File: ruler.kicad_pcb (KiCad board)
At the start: 2 copper layers, 170.8 x 38.1 mm, 25 parts, among them J1 USB_OTG, J2 Conn_01x01, SW1 KMR2, SW2 EVQPE1, SW3 B3U1000P, SW4 FSMCT, SW5 TL3315, SW6 FSM2JSM, SW7 JS202011SCQN

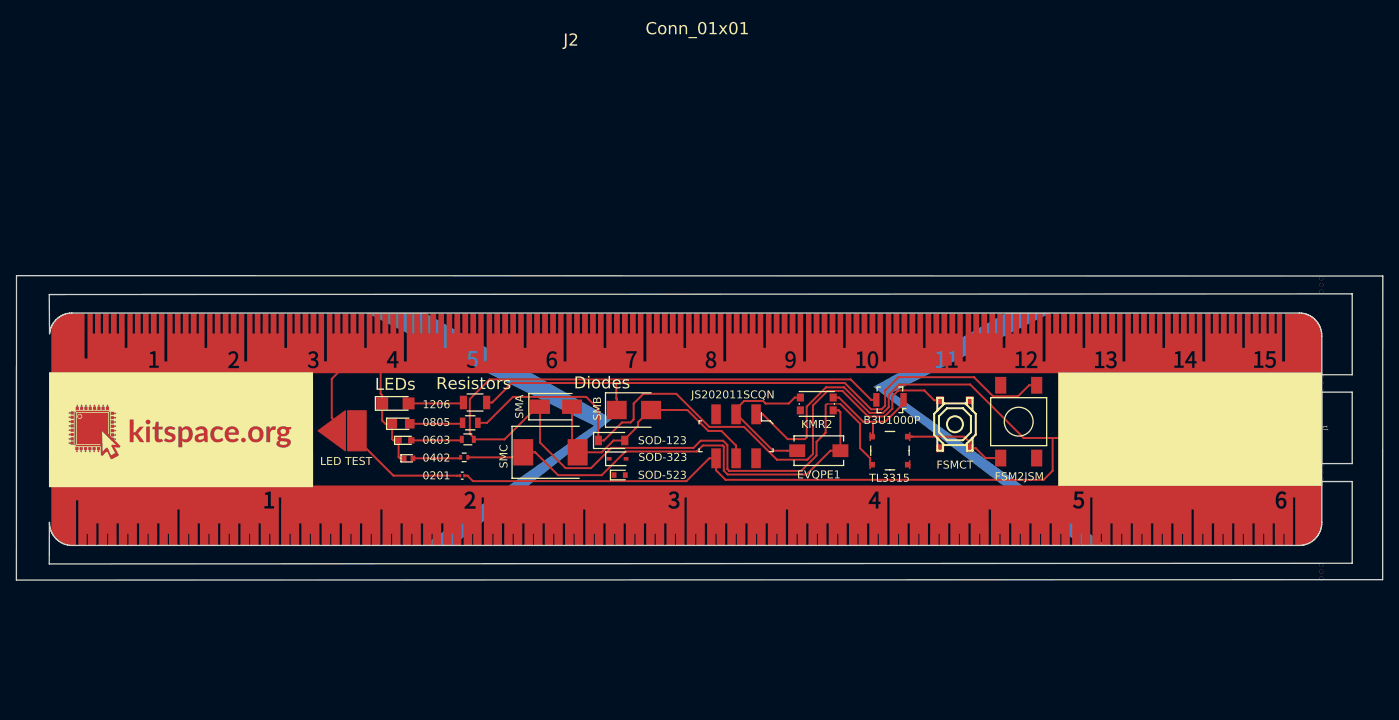
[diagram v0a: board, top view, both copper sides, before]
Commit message: Add inductors, caps, transitors and ICs
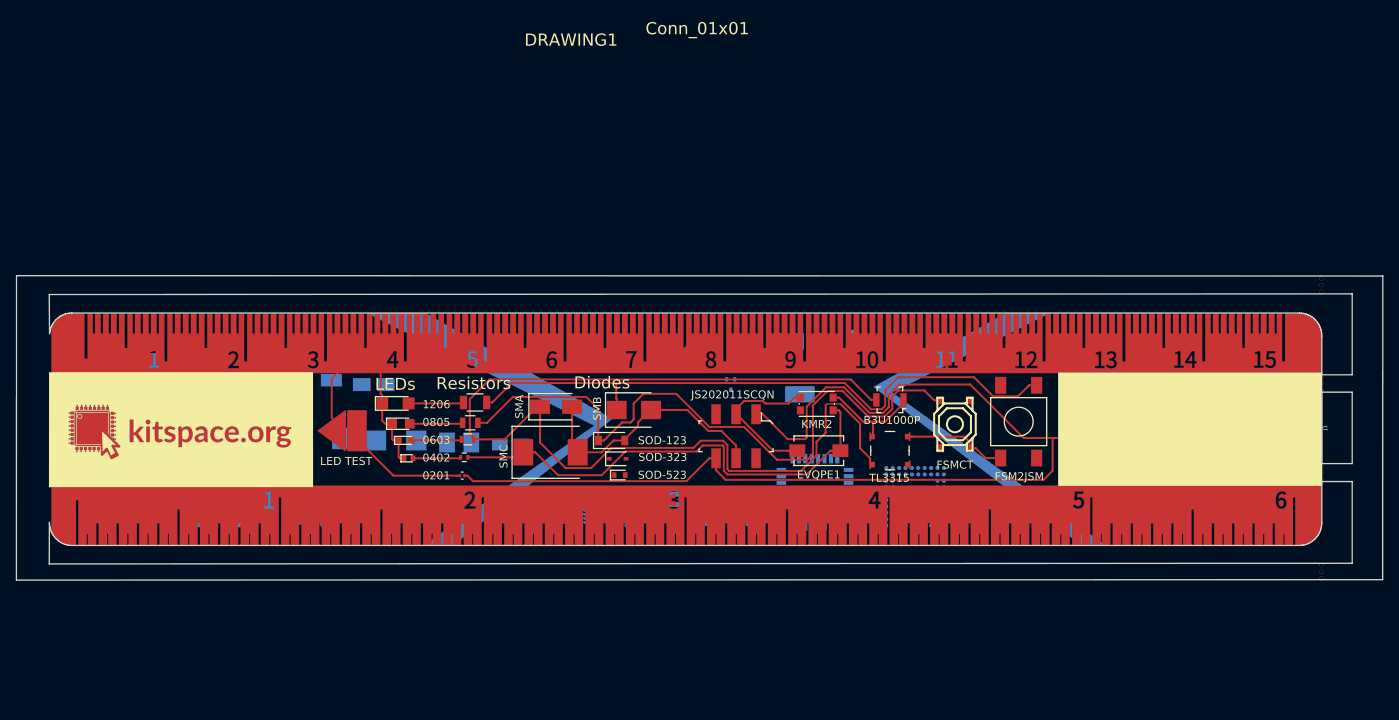
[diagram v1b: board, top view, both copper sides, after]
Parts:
- removed J2: Conn_01x01, drawing:drawing
- added C1: 3x5.3mm, KiCad/Capacitors_SMD.pretty:CP_Elec_3x5.3, B.Cu at (105.9, 99.5)
- added C2: 4x5.8mm, KiCad/Capacitors_SMD.pretty:CP_Elec_4x5.8, B.Cu at (98.8, 98.9)
- added C3: 5x5.8mm, KiCad/Capacitors_SMD.pretty:CP_Elec_5x5.8, B.Cu at (90.7, 98.5)
- added C4: 8x5.4mm, KiCad/Capacitors_SMD.pretty:CP_Elec_8x5.4, B.Cu at (80.8, 96.8)
- added C5: A/3216, KiCad/Capacitors_Tantalum_SMD.pretty:CP_Tantalum_Case-A_EIA-3216-18_Reflow, B.Cu at (123.0, 106.9)
- added C6: B/3528, KiCad/Capacitors_Tantalum_SMD.pretty:CP_Tantalum_Case-B_EIA-3528-21_Reflow, B.Cu at (116.6, 106.7)
- added C7: C/6032, KiCad/Capacitors_Tantalum_SMD.pretty:CP_Tantalum_Case-C_EIA-6032-28_Reflow, B.Cu at (108.7, 106.4)
- added C8: D/7343, KiCad/Capacitors_Tantalum_SMD.pretty:CP_Tantalum_Case-D_EIA-7343-31_Reflow, B.Cu at (98.8, 106.2)
- added DRAWING1: Conn_01x01, drawing:drawing, F.Cu at (148.5, 105.0)
- added L1: 1008, jnedbal/jakub.pretty:Inductor_1008, B.Cu at (106.7, 116.5)
- added L2: SRU8043, custom:Inductor_Bourns-SRU8043, B.Cu at (77.0, 113.2)
- added L3: 4040, KiCad/Inductors.pretty:Inductor_Taiyo-Yuden_MD-4040, B.Cu at (101.2, 115.3)
- added L4: 5050, KiCad/Inductors.pretty:Inductor_Taiyo-Yuden_MD-5050, B.Cu at (94.7, 114.8)
- added L5: 60xx, KiCad/Inductors.pretty:Inductor_Taiyo-Yuden_NR-60xx, B.Cu at (87.0, 114.3)
- added Q1: Q_NMOS_DGS, adamgreig/agg-kicad/agg.pretty:SOT-23, B.Cu at (166.8, 93.8)
- added Q2: Q_NMOS_DGS, adamgreig/agg-kicad/agg.pretty:SOT-323, B.Cu at (144.2, 95.0)
- added Q3: Q_NMOS_DGS, adamgreig/agg-kicad/agg.pretty:SOT-883-B, B.Cu at (151.4, 93.8)
- added Q4: Q_NMOS_DGS, digikey/digikey-kicad-library/digikey-footprints.pretty:SOT-523, B.Cu at (150.5, 98.8)
- added Q5: Q_NMOS_DGS, ep092/library_toni.pretty:SOT223_GND_VO_VI, B.Cu at (159.2, 97.3)
- added U1: Conn_01x01, KiCad/Housings_DFN_QFN.pretty:QFN-16-1EP_3x3mm_Pitch0.5mm, B.Cu at (131.0, 115.9)
- added U2: Conn_01x01, adamgreig/agg-kicad/agg.pretty:LQFP-32, B.Cu at (161.1, 112.9)
- added U3: Conn_01x01, adamgreig/agg-kicad/agg.pretty:SOIC-8, B.Cu at (140.8, 115.0)
- added U4: Conn_01x01, KiCad/SMD_Packages.pretty:BGA-64-0.8mm, B.Cu at (173.6, 113.5)
- added U5: Conn_01x01, KiCad/Housings_SSOP.pretty:TSSOP-16_4.4x5mm_Pitch0.65mm, B.Cu at (150.2, 114.6)

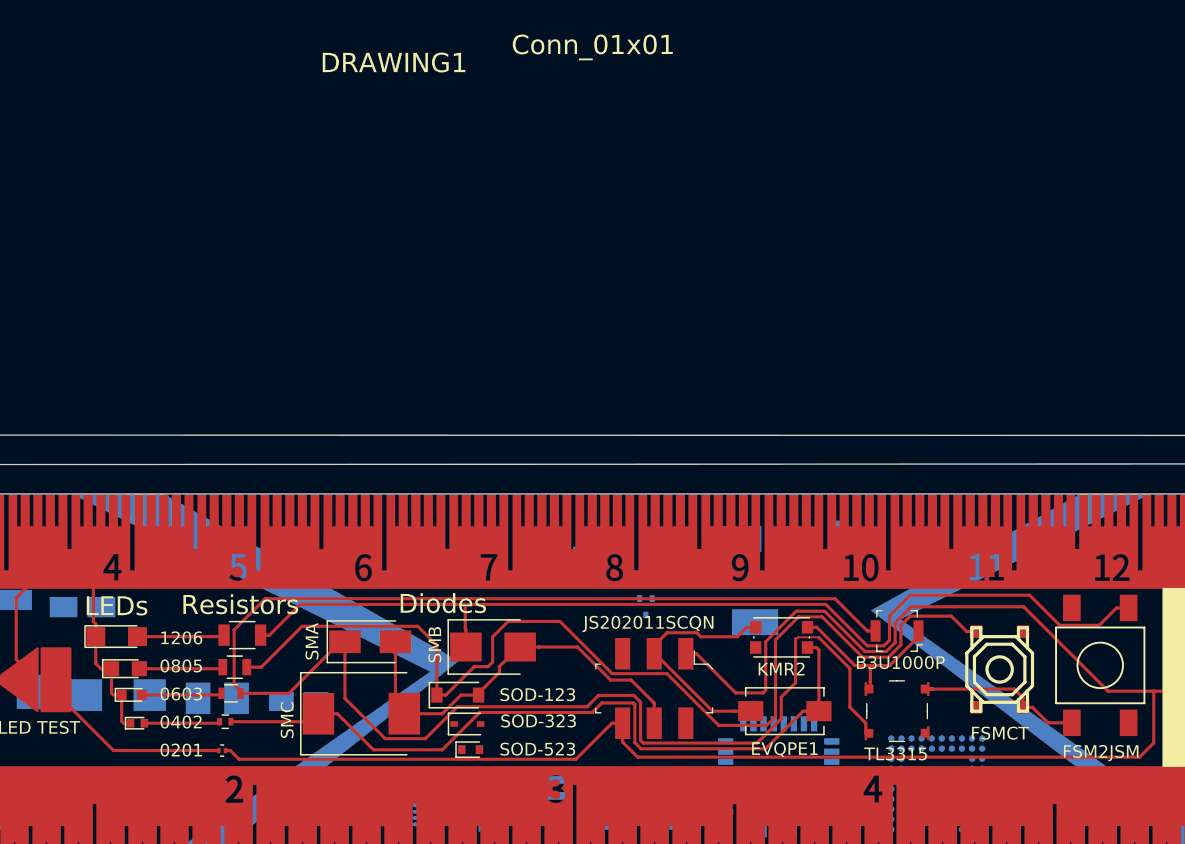
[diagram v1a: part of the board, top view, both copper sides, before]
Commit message: Change text to inkscape versions
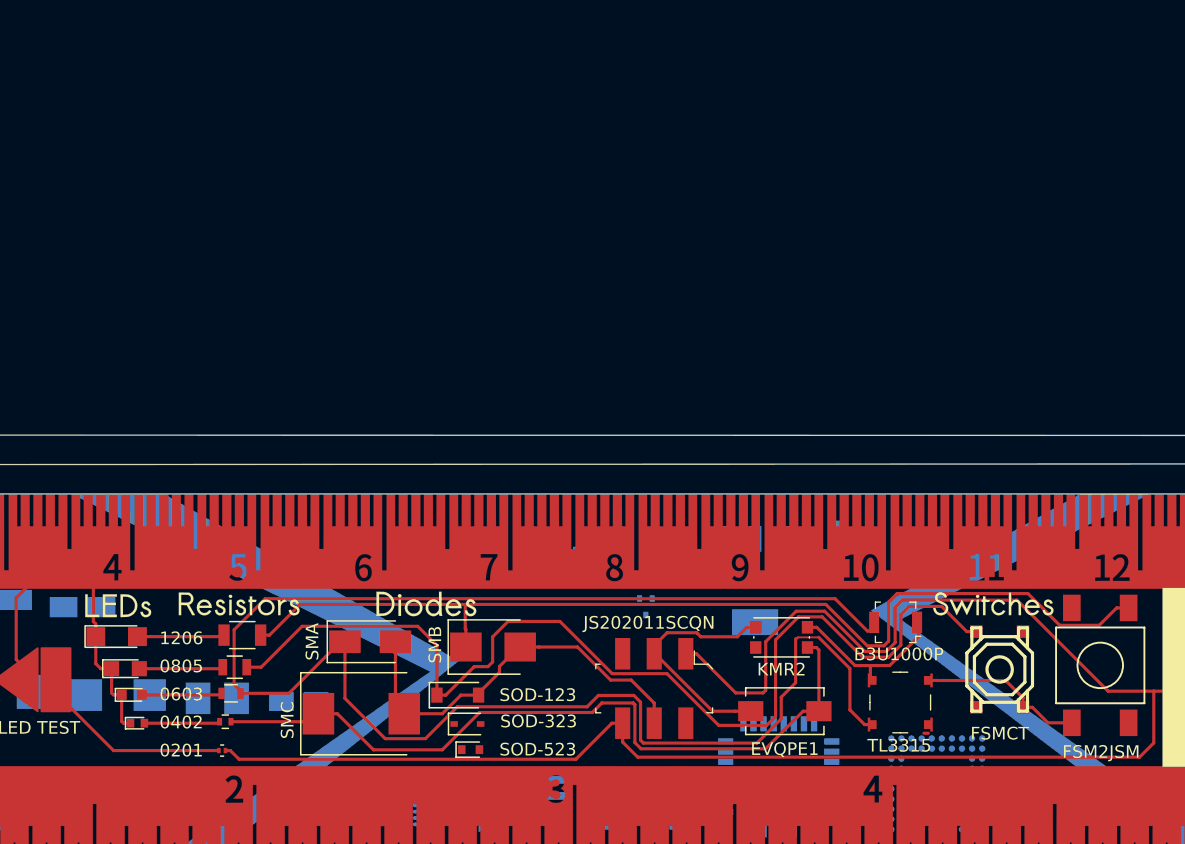
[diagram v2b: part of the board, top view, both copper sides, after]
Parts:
- added DRAWING2: Conn_01x01, drawings:leds_text, F.Cu at (117.6, 98.4)
- added DRAWING3: Conn_01x01, drawings:resistors_text, F.Cu at (119.2, 99.5)
- added DRAWING4: Conn_01x01, drawings:diodes_text, F.Cu at (134.8, 99.6)
- added DRAWING5: Conn_01x01, drawings:switches_text, F.Cu at (179.0, 99.5)
- DRAWING1: footprint drawing:drawing -> drawings:ruler
- moved SW5 0.73 mm to (170.7, 107.0)
- moved SW3 0.70 mm to (170.3, 100.7)
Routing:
- net SW_V+: track 46.4 -> 45.1 mm
- net +5V: track 160.1 -> 161.3 mm
- net Net-(D4-Pad1): track 81.9 -> 83.0 mm
- net Net-(D2-Pad1): track 79.0 -> 79.8 mm
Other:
- board text removed: "Diodes"
- board text removed: "LEDs"
- board text removed: "Resistors"

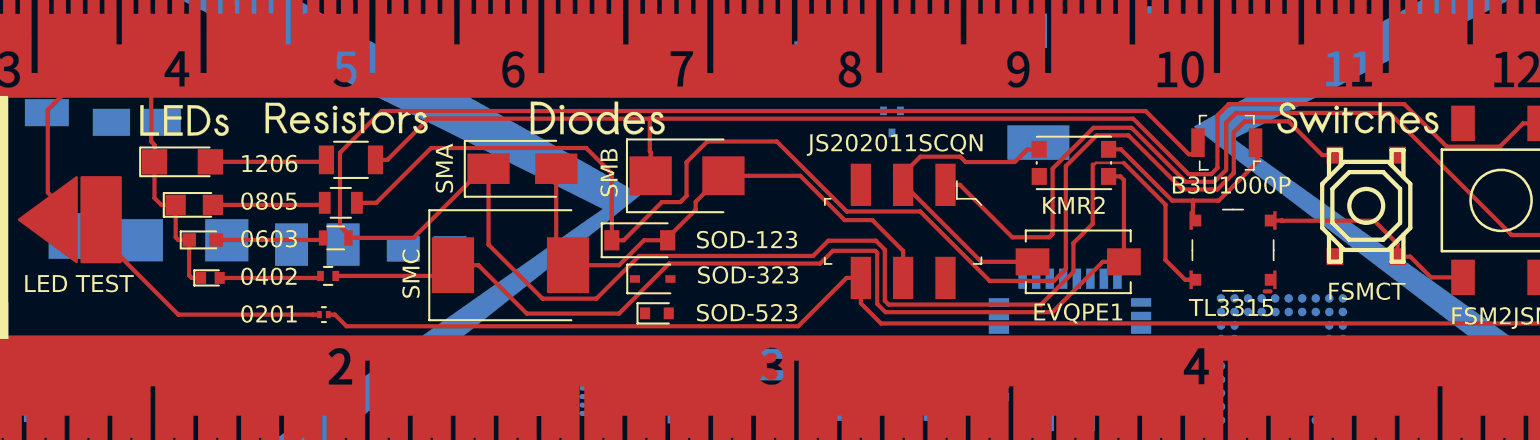
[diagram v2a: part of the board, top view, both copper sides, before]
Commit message: Adjust title texts
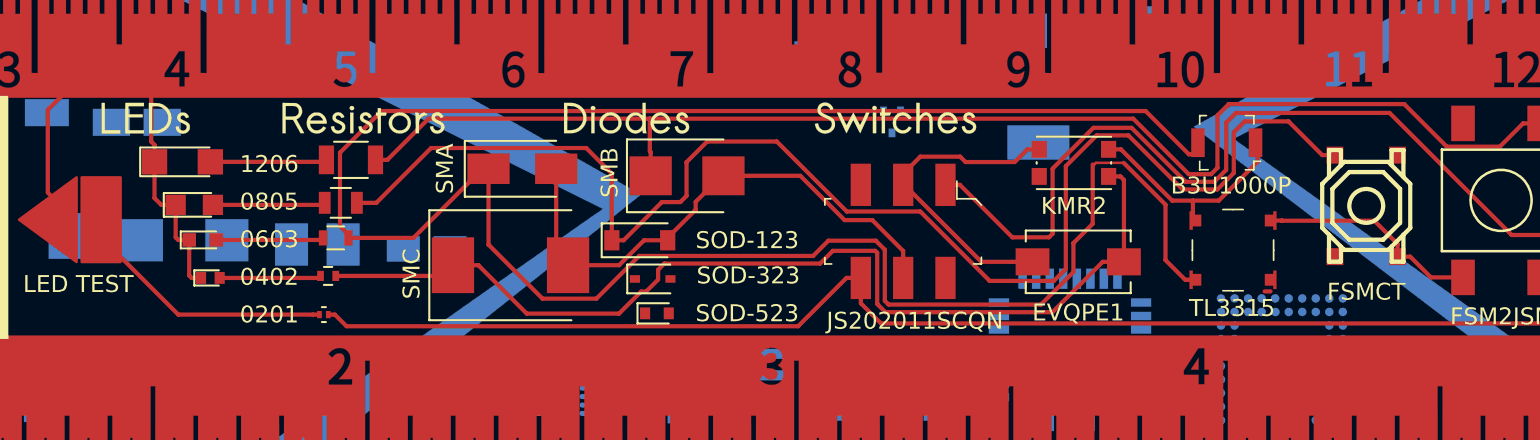
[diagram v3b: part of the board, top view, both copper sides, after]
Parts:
- moved DRAWING5 27.3 mm to (151.7, 99.5)
- moved DRAWING2 2.29 mm to (115.3, 98.3)
- moved DRAWING3 0.99 mm to (120.2, 99.5)
- moved DRAWING4 0.06 mm to (134.8, 99.5)

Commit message: Add more text
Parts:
- added DRAWING10: Conn_01x01, drawings:tantalum_text, B.Cu at (68.6, 114.3)
- added DRAWING11: Conn_01x01, drawings:electrolytic_text, B.Cu at (75.2, 101.6)
- added DRAWING12: Conn_01x01, drawings:vscore, B.Cu at (65.3, 97.3)
- added DRAWING6: Conn_01x01, drawings:capacitors_text, B.Cu at (77.5, 93.0)
- added DRAWING7: Conn_01x01, drawings:transistors_text, B.Cu at (150.6, 92.8)
- added DRAWING8: Conn_01x01, drawings:ics_text, B.Cu at (153.2, 106.9)
- added DRAWING9: Conn_01x01, drawings:inductors_text, B.Cu at (69.1, 139.7)
- moved C6 24.8 mm to (92.7, 113.3)
- moved C7 24.8 mm to (84.8, 113.0)
- moved C5 24.8 mm to (99.2, 113.5)
- moved C8 24.8 mm to (74.9, 112.8)
- moved L2 22.2 mm to (74.7, 135.3)
- moved L1 22.2 mm to (104.4, 138.6)
- moved L3 22.2 mm to (99.0, 137.4)
- moved L4 22.2 mm to (92.4, 136.9)
- moved L5 22.2 mm to (84.7, 136.4)
- moved Q1 14.5 mm to (152.7, 97.4), turned to 270 degrees
- moved Q3 11.6 mm to (140.5, 97.9)
- moved Q4 7.58 mm to (143.2, 97.0)
- moved C1 6.53 mm to (107.4, 105.8)
- moved C2 6.53 mm to (100.3, 105.2)
- moved C3 6.53 mm to (92.2, 104.9)
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
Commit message: Adjust led tester text
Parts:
- LED1: value LED TEST PADS -> LED Tester
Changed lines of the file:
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@@
   (page A4)
   (layers
-    (0 F.Cu signal hide)
-    (31 B.Cu signal)
+    (0 F.Cu signal)
+    (31 B.Cu signal hide)
     (32 B.Adhes user hide)
     (33 F.Adhes user hide)
-    (34 B.Paste user)
-    (35 F.Paste user hide)
-    (36 B.SilkS user)
-    (37 F.SilkS user hide)
-    (38 B.Mask user)
-    (39 F.Mask user hide)
+    (34 B.Paste user hide)
+    (35 F.Paste user)
+    (36 B.SilkS user hide)
+    (37 F.SilkS user)
+    (38 B.Mask user hide)
+    (39 F.Mask user)
     (40 Dwgs.User user hide)
     (41 Cmts.User user hide)
@@
     (44 Edge.Cuts user)
     (45 Margin user hide)
-    (46 B.CrtYd user)
-    (47 F.CrtYd user hide)
-    (48 B.Fab user)
-    (49 F.Fab user hide)
+    (46 B.CrtYd user hide)
+    (47 F.CrtYd user)
+    (48 B.Fab user hide)
+    (49 F.Fab user)
   )
   (setup
@@
     (pad_to_mask_clearance 0.2)
     (aux_axis_origin 0 0)
-    (visible_elements FFFFE57F)
+    (visible_elements FFFEE37F)
     (pcbplotparams
       (layerselection 0x010f0_ffffffff)
@@
       (effects (font (size 0.29972 0.29972) (thickness 0.0635)))
     )
-    (fp_text value "LED TEST PADS" (at 0 1.30048 180) (layer F.Fab)
+    (fp_text value "LED Tester" (at 0 1.30048 180) (layer F.Fab)
       (effects (font (size 0.29972 0.29972) (thickness 0.0635)))
     )
@@
       (effects (font (size 0.29972 0.29972) (thickness 0.0635)))
     )
-    (fp_text user "LED TEST" (at 0 -3.81) (layer F.SilkS)
+    (fp_text user "LED Tester" (at -0.40916 -3.81) (layer F.SilkS)
       (effects (font (size 1 1) (thickness 0.25)))
     )

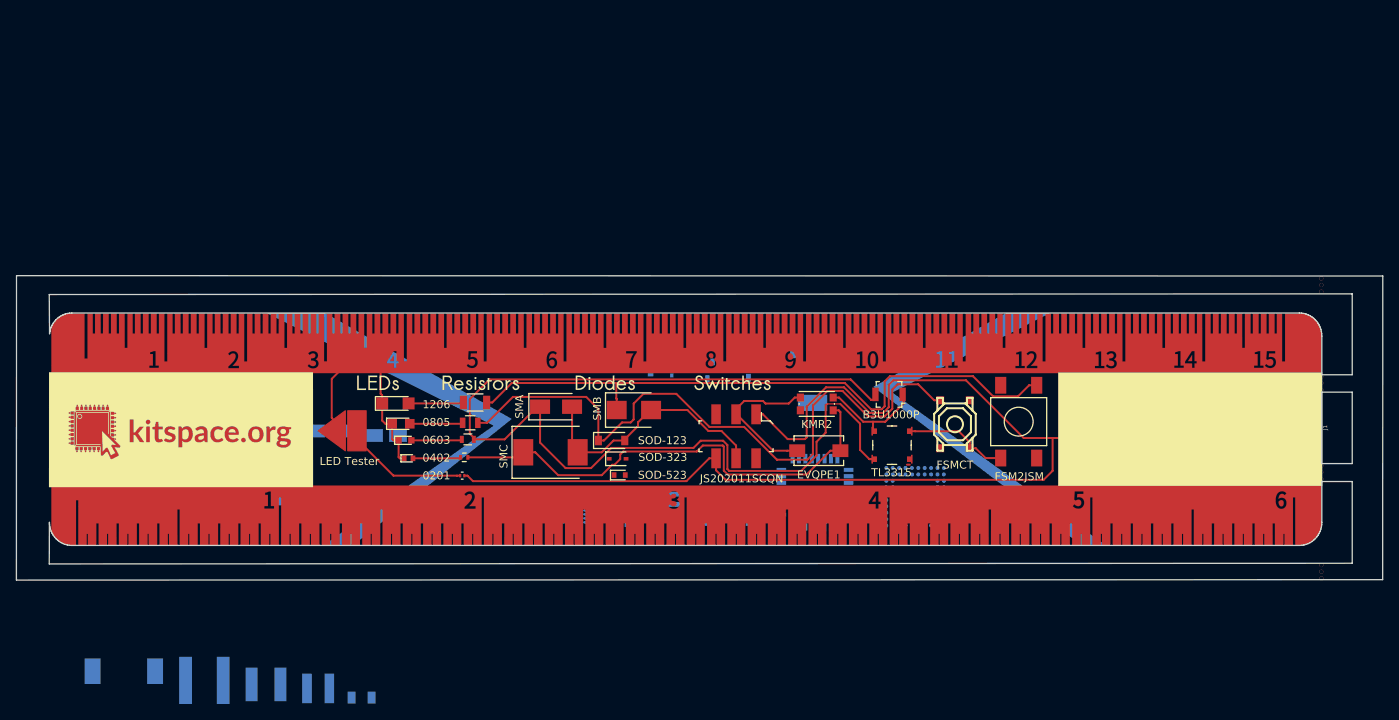
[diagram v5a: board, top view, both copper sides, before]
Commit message: Add more ICs
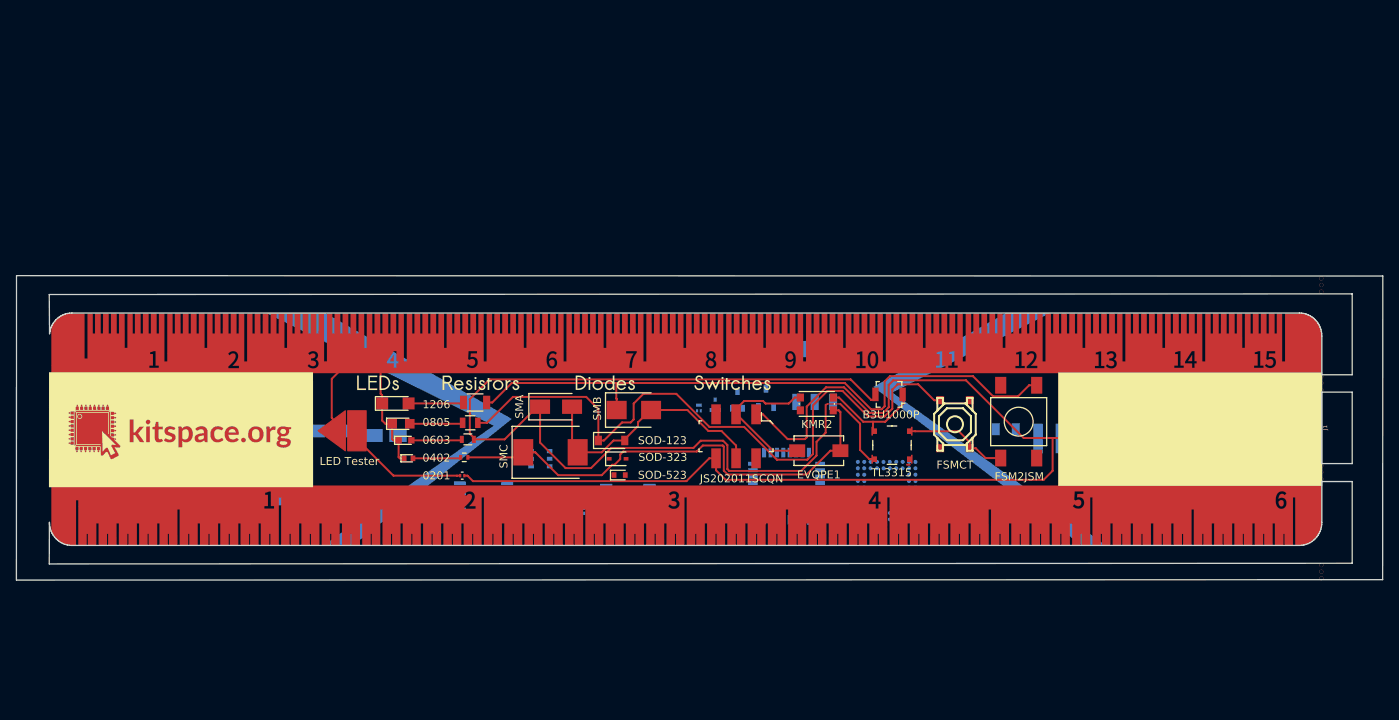
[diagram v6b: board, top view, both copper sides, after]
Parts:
- added U6: MSOIC, smisioto.eu/kicad_libs/modules/w_smd_dil.pretty:msoic-8, B.Cu at (129.5, 114.6)
- added U7: TSOP-0.95mm, KiCad/Housings_SSOP.pretty:TSOP-6_1.65x3.05mm_Pitch0.95mm, B.Cu at (126.7, 108.7)
- Q1: value Q_NMOS_DGS -> SOT23
- Q2: value Q_NMOS_DGS -> SOT323
- Q3: value Q_NMOS_DGS -> SOT883
- Q4: value Q_NMOS_DGS -> SOT523
- Q5: value Q_NMOS_DGS -> SOT223
- U1: value Conn_01x01 -> QFN-0.5mm
- U2: value Conn_01x01 -> LQFP
- U3: value Conn_01x01 -> SOIC
- U4: value Conn_01x01 -> BGA-0.8mm
- U5: value Conn_01x01 -> TSSOP-0.65mm
- moved DRAWING9 155.2 mm to (220.2, 103.9), turned to 90 degrees
- moved L2 142.5 mm to (214.6, 108.3), turned to 0 degrees
- moved L5 123.3 mm to (204.6, 107.2), turned to 180 degrees
- moved L4 108.7 mm to (196.9, 106.7), turned to 180 degrees
- moved L3 96.6 mm to (190.3, 106.2), turned to 180 degrees
- moved L1 87.2 mm to (184.9, 105.0), turned to 180 degrees
- moved U5 30.6 mm to (119.6, 114.0)
- moved U1 16.1 mm to (147.1, 114.8), turned to 180 degrees
- moved DRAWING8 12.4 mm to (141.2, 110.2)
- moved Q4 7.81 mm to (148.6, 102.6), turned to 180 degrees
- moved Q3 7.54 mm to (146.6, 102.4), turned to 180 degrees
- moved Q2 5.28 mm to (151.4, 101.3), turned to 90 degrees
- moved Q1 4.26 mm to (154.9, 101.1), turned to 90 degrees
- moved U2 3.64 mm to (157.5, 112.1)
- moved U4 3.64 mm to (170.0, 112.7)
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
